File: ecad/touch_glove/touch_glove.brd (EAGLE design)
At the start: 80 x 38.4 mm, 376 parts, among them IC1 DRV8662, J1 VERT MALE 2.54MM, J2 VERT MALE 2.54MM, J3 VERT MALE 2.54MM, J4 VERT MALE 2.54MM, J5 VERT MALE 2.54MM, J6 PTH VERT MALE, J7 PTH VERT MALE, J8 PTH VERT MALE, J9 PTH VERT MALE, Q1 MCH3474 4A/30V, Q2 MCH3474 4A/30V, Q3 MCH3474 4A/30V, Q4 MCH3474 4A/30V, Q5 MCH3474 4A/30V, Q6 MCH3474 4A/30V, SW1 4A/28V, SW2 25mA/24V

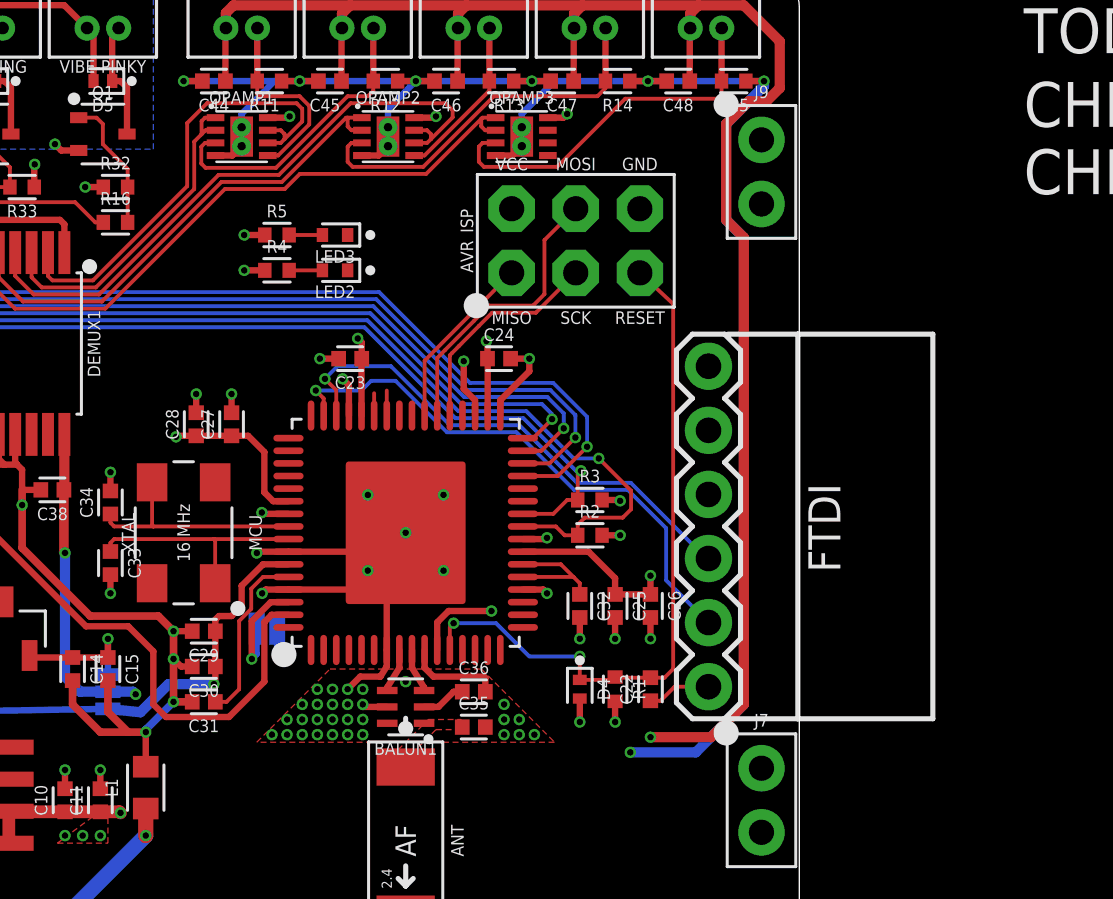
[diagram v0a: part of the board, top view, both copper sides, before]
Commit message: Create mcu to unity example code.  Create schematics for master thesis.  Edit robotic arm and touch glove pcb.
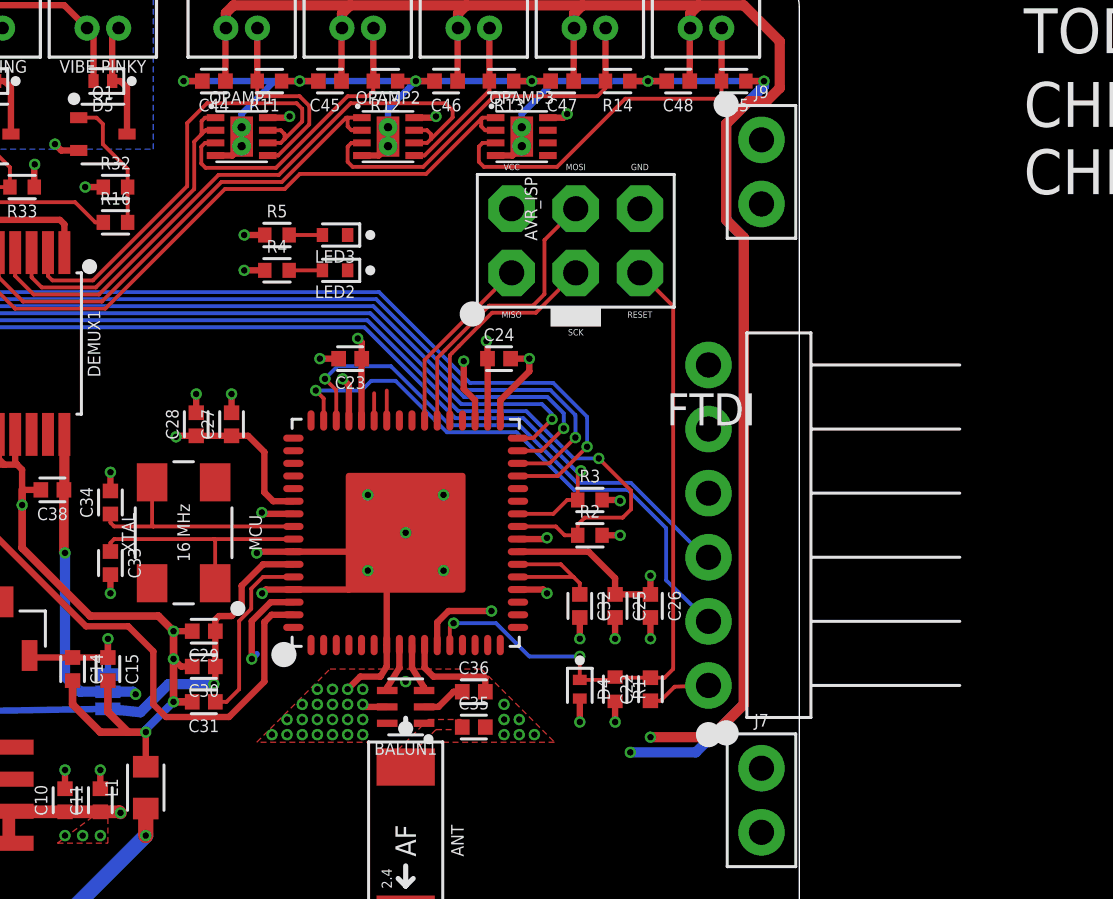
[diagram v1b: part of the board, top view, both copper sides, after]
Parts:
- removed JP2: JUMPER_SMD_2-PAD_NO_SILK, _connectors:SMT-JUMPER_2_NO_SILK
- AVR_ISP: value PTH VERT MALE -> AVR ISP; device _connectors:HDRV6W64P254_2X3_762X483X838B_AVR-ISP -> _connectors:HDRV6W64P254_2X3_762X508X838B
- FTDI: value FTDI -> PTH RA VERT MALE; device _connectors:FTDI_BASIC-6PIN-MALE-RA -> _connectors:HDRRA6W64P254_1X6_1524X254X254B_FTDI
- moved AVR_ISP 2.84 mm to (71.1, 27.9)
- turned FTDI to 90 degrees
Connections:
- removed net AREF: JP2.2, MCU.62
- net A1.8V: now also MCU.62
- net VSENSOR: no longer JP2.1
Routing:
- net AREF: track 4.55 -> 0.00 mm, vias 1 -> 0
- net A1.8V: track 5.30 -> 9.04 mm, vias 1 -> 2
- net GND: track 65.9 -> 66.9 mm
- net VSENSOR: track 138.6 -> 137.6 mm
- net VCC: track 50.3 -> 51.1 mm

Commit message: Create PCA9685Servo library.  Touch up Touch Glove PCB.  Major work completed on ET Extension.
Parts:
- removed C16, C19, C37, C49, C63, C64, C66, C67, C68, C69, C70, C76, C78, C80: 0.1uF/50V, _capacitors:CAPC1005X55_SMD-0402
- removed C17, C20, C71, C72, C73, C75, C77, C79: 10uF/6.3V, _capacitors:CAPC1005X55_SMD-0402
- removed C61: 0.1uF/25V, _capacitors:CAPC1608X95
- removed C62: 0.1uF/250V, _capacitors:CAPC2012X95_SMD-0805
- removed C65: 100uF/10V, _capacitors:CAPCP3216X160
- removed C74: 4.7uF/10V/0402, _capacitors:CAPC1005X55_SMD-0402
- removed ET_INDEX_PIXEL1-1, ET_INDEX_PIXEL1-10, ET_INDEX_PIXEL1-11, ET_INDEX_PIXEL1-12, ET_INDEX_PIXEL1-13, ET_INDEX_PIXEL1-14, ET_INDEX_PIXEL1-15, ET_INDEX_PIXEL1-16, ET_INDEX_PIXEL1-17, ET_INDEX_PIXEL1-18, ET_INDEX_PIXEL1-19, ET_INDEX_PIXEL1-2, ET_INDEX_PIXEL1-20, ET_INDEX_PIXEL1-3, ET_INDEX_PIXEL1-4, ET_INDEX_PIXEL1-5, ET_INDEX_PIXEL1-6, ET_INDEX_PIXEL1-7, ET_INDEX_PIXEL1-8, ET_INDEX_PIXEL1-9, ET_INDEX_PIXEL2-1, ET_INDEX_PIXEL2-10, ET_INDEX_PIXEL2-11, ET_INDEX_PIXEL2-12, ET_INDEX_PIXEL2-13, ET_INDEX_PIXEL2-14, ET_INDEX_PIXEL2-15, ET_INDEX_PIXEL2-16, ET_INDEX_PIXEL2-17, ET_INDEX_PIXEL2-18, ET_INDEX_PIXEL2-19, ET_INDEX_PIXEL2-2, ET_INDEX_PIXEL2-20, ET_INDEX_PIXEL2-3, ET_INDEX_PIXEL2-4, ET_INDEX_PIXEL2-5, ET_INDEX_PIXEL2-6, ET_INDEX_PIXEL2-7, ET_INDEX_PIXEL2-8, ET_INDEX_PIXEL2-9, ET_INDEX_PIXEL3-1, ET_INDEX_PIXEL3-10, ET_INDEX_PIXEL3-11, ET_INDEX_PIXEL3-12, ET_INDEX_PIXEL3-13, ET_INDEX_PIXEL3-14, ET_INDEX_PIXEL3-15, ET_INDEX_PIXEL3-16, ET_INDEX_PIXEL3-17, ET_INDEX_PIXEL3-18, ET_INDEX_PIXEL3-19, ET_INDEX_PIXEL3-2, ET_INDEX_PIXEL3-20, ET_INDEX_PIXEL3-3, ET_INDEX_PIXEL3-4, ET_INDEX_PIXEL3-5, ET_INDEX_PIXEL3-6, ET_INDEX_PIXEL3-7, ET_INDEX_PIXEL3-8, ET_INDEX_PIXEL3-9, ET_INDEX_PIXEL4-1, ET_INDEX_PIXEL4-10, ET_INDEX_PIXEL4-11, ET_INDEX_PIXEL4-12, ET_INDEX_PIXEL4-13, ET_INDEX_PIXEL4-14, ET_INDEX_PIXEL4-15, ET_INDEX_PIXEL4-16, ET_INDEX_PIXEL4-17, ET_INDEX_PIXEL4-18, ET_INDEX_PIXEL4-19, ET_INDEX_PIXEL4-2, ET_INDEX_PIXEL4-20, ET_INDEX_PIXEL4-3, ET_INDEX_PIXEL4-4, ET_INDEX_PIXEL4-5, ET_INDEX_PIXEL4-6, ET_INDEX_PIXEL4-7, ET_INDEX_PIXEL4-8, ET_INDEX_PIXEL4-9: SPST-NO 170mA 250V, _relay:SOP254P609X203-4
- removed IC1: DRV8662, _special:QFN50P400X400X100-21T270
- removed J1, J2, J3, J4, J5: VERT MALE 2.54MM, _connectors:HDRV16W64P254_1X16_4064X254X838B
- removed L3: 4.7uH/1.4A, _inductors:INDC2520X100
- removed L4: 10uH/380mA, _inductors:INDC1608X60-0603
- removed NFET1: 2N7002DW, _transistors:SOT65P230X110-6
- removed OPAMP4: TLV2361_GP_20MA_7MHZ, _op_amps:SOT95P280X145-5
- removed POT1: 100K, _resistors:POTENTIOMETER_SQ-L5-W4.5-H2.3
- removed PWM_DRIVER2, PWM_DRIVER3, PWM_DRIVER4, PWM_DRIVER5, PWM_DRIVER6: PCA9685, _special:SOP65P650X110-28
- removed R100, R101, R102, R103, R104, R105, R106, R107, R108, R109, R110, R111, R112, R113, R114, R115, R116, R117, R118, R119, R120, R121, R122, R123, R124, R125, R126, R127, R128, R129, R130, R131, R132, R133, R134, R135, R49, R57, R58, R59, R60, R61, R62, R63, R64, R65, R66, R67, R68, R69, R70, R71, R72, R73, R74, R75, R76, R77, R78, R79, R80, R81, R82, R83, R84, R85, R86, R87, R88, R89, R90, R91, R92, R93, R94, R95, R96, R97, R98, R99: 1K, _resistors:RESC1005X35_SMD-0402
- removed R136, R137, R54, R55, R56: 10K, _resistors:RESC1005X35_SMD-0402
- removed R16, R17, R18, R19, R20, R21, R22, R23, R24, R25, R26, R27, R28, R29, R30, R31: 100, _resistors:RESC1005X35_SMD-0402
- removed R50: 768K, _resistors:RESC1005X35_SMD-0402
- removed R51: 35.7K, _resistors:RESC1005X35_SMD-0402
- removed R52: 20K, _resistors:RESC1005X35_SMD-0402
- removed R53: 41.2K, _resistors:RESC1005X35_SMD-0402
- removed REXT: 7.5K, _resistors:RESC1005X35_SMD-0402
- removed SW2: 25mA/24V, _switches:SW_SLIDE_ARRAY-3_L9.6-W7.5-H4.5
- removed VREG-MCU1: TPS76833QDR 1A/3.3V, _ic_power:SOIC127P600X265-8
- removed VREG2: NCP1729 50mA, _ic_power:SOT95P275X100-6
- removed VREG3: TPS62202 300mA 1.8V, _ic_power:SOT95P280X145-5
- moved C8 3.04 mm to (22.0, 13.6)
- moved C9 3.03 mm to (22.0, 14.9)
- moved C2 3.00 mm to (23.0, 10.6)
- moved VREG-TEC 3.00 mm to (15.3, 19.8)
- moved D3 2.90 mm to (24.4, 19.8)
- moved C18 2.83 mm to (32.1, 17.4), turned to 180 degrees
- moved VREG-VIBE 2.38 mm to (30.3, 12.4)
- moved C3 2.30 mm to (30.3, 7.40)
- moved C7 2.30 mm to (33.9, 8.70)
- moved U$1 2.30 mm to (33.2, 7.00)
- moved C6 2.30 mm to (33.9, 7.40)
- moved R48 2.21 mm to (37.0, 8.20)
- moved LED1 2.20 mm to (37.0, 6.00)
- moved D2 2.18 mm to (35.9, 12.4)
- moved C50 1.94 mm to (41.4, 19.6)
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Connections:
- net AVCC renamed A3.3V
- removed net -1.8V: C72.1, OPAMP4.2, VREG2.1
- removed net C+: C71.1, VREG2.6
- removed net C-: C71.2, VREG2.3
- removed net EN: IC1.20, R54.2, SW2.S3
- removed net FB: IC1.3, R50.1, R51.2, R52.2, R53.2
- removed net GAIN0: IC1.18, NFET1.5, R55.2, SW2.S2
- removed net GAIN1: IC1.19, NFET1.2, R56.2, SW2.S1
- removed net IN+: C64.1, OPAMP4.4, POT1.1, POT1.2, R136.2
- removed net INDEX_IN1-1: ET_INDEX_PIXEL1-1.1, ET_INDEX_PIXEL1-13.1, ET_INDEX_PIXEL1-17.1, ET_INDEX_PIXEL1-5.1, ET_INDEX_PIXEL1-9.1, PWM_DRIVER2.6, PWM_DRIVER3.6, PWM_DRIVER4.6, PWM_DRIVER5.6, PWM_DRIVER6.6
- removed net INDEX_IN1-2: ET_INDEX_PIXEL1-10.1, ET_INDEX_PIXEL1-14.1, ET_INDEX_PIXEL1-18.1, ET_INDEX_PIXEL1-2.1, ET_INDEX_PIXEL1-6.1, PWM_DRIVER2.7, PWM_DRIVER3.7, PWM_DRIVER4.7, PWM_DRIVER5.7, PWM_DRIVER6.7
- removed net INDEX_IN1-3: ET_INDEX_PIXEL1-11.1, ET_INDEX_PIXEL1-15.1, ET_INDEX_PIXEL1-19.1, ET_INDEX_PIXEL1-3.1, ET_INDEX_PIXEL1-7.1, PWM_DRIVER2.8, PWM_DRIVER3.8, PWM_DRIVER4.8, PWM_DRIVER5.8, PWM_DRIVER6.8
- removed net INDEX_IN1-4: ET_INDEX_PIXEL1-12.1, ET_INDEX_PIXEL1-16.1, ET_INDEX_PIXEL1-20.1, ET_INDEX_PIXEL1-4.1, ET_INDEX_PIXEL1-8.1, PWM_DRIVER2.9, PWM_DRIVER3.9, PWM_DRIVER4.9, PWM_DRIVER5.9, PWM_DRIVER6.9
- removed net INDEX_IN2-1: ET_INDEX_PIXEL2-1.1, ET_INDEX_PIXEL2-11.1, ET_INDEX_PIXEL2-15.1, ET_INDEX_PIXEL2-19.1, ET_INDEX_PIXEL2-7.1, PWM_DRIVER2.10, PWM_DRIVER3.10, PWM_DRIVER4.10, PWM_DRIVER5.10, PWM_DRIVER6.10
- removed net INDEX_IN2-2: ET_INDEX_PIXEL2-10.1, ET_INDEX_PIXEL2-14.1, ET_INDEX_PIXEL2-18.1, ET_INDEX_PIXEL2-2.1, ET_INDEX_PIXEL2-6.1, PWM_DRIVER2.11, PWM_DRIVER3.11, PWM_DRIVER4.11, PWM_DRIVER5.11, PWM_DRIVER6.11
- removed net INDEX_IN2-3: ET_INDEX_PIXEL2-13.1, ET_INDEX_PIXEL2-17.1, ET_INDEX_PIXEL2-3.1, ET_INDEX_PIXEL2-5.1, ET_INDEX_PIXEL2-9.1, PWM_DRIVER2.12, PWM_DRIVER3.12, PWM_DRIVER4.12, PWM_DRIVER5.12, PWM_DRIVER6.12
- removed net INDEX_IN2-4: ET_INDEX_PIXEL2-12.1, ET_INDEX_PIXEL2-16.1, ET_INDEX_PIXEL2-20.1, ET_INDEX_PIXEL2-4.1, ET_INDEX_PIXEL2-8.1, PWM_DRIVER2.13, PWM_DRIVER3.13, PWM_DRIVER4.13, PWM_DRIVER5.13, PWM_DRIVER6.13
- removed net INDEX_IN3-1: ET_INDEX_PIXEL3-1.1, ET_INDEX_PIXEL3-13.1, ET_INDEX_PIXEL3-17.1, ET_INDEX_PIXEL3-5.1, ET_INDEX_PIXEL3-9.1, PWM_DRIVER2.15, PWM_DRIVER3.15, PWM_DRIVER4.15, PWM_DRIVER5.15, PWM_DRIVER6.15
- removed net INDEX_IN3-2: ET_INDEX_PIXEL3-10.1, ET_INDEX_PIXEL3-14.1, ET_INDEX_PIXEL3-18.1, ET_INDEX_PIXEL3-2.1, ET_INDEX_PIXEL3-6.1, PWM_DRIVER2.16, PWM_DRIVER3.16, PWM_DRIVER4.16, PWM_DRIVER5.16, PWM_DRIVER6.16
- removed net INDEX_IN3-3: ET_INDEX_PIXEL3-11.1, ET_INDEX_PIXEL3-15.1, ET_INDEX_PIXEL3-19.1, ET_INDEX_PIXEL3-3.1, ET_INDEX_PIXEL3-7.1, PWM_DRIVER2.17, PWM_DRIVER3.17, PWM_DRIVER4.17, PWM_DRIVER5.17, PWM_DRIVER6.17
- removed net INDEX_IN3-4: ET_INDEX_PIXEL3-12.1, ET_INDEX_PIXEL3-16.1, ET_INDEX_PIXEL3-20.1, ET_INDEX_PIXEL3-4.1, ET_INDEX_PIXEL3-8.1, PWM_DRIVER2.18, PWM_DRIVER3.18, PWM_DRIVER4.18, PWM_DRIVER5.18, PWM_DRIVER6.18
- removed net INDEX_IN4-1: ET_INDEX_PIXEL4-1.1, ET_INDEX_PIXEL4-13.1, ET_INDEX_PIXEL4-17.1, ET_INDEX_PIXEL4-5.1, ET_INDEX_PIXEL4-9.1, PWM_DRIVER2.19, PWM_DRIVER3.19, PWM_DRIVER4.19, PWM_DRIVER5.19, PWM_DRIVER6.19
- removed net INDEX_IN4-2: ET_INDEX_PIXEL4-10.1, ET_INDEX_PIXEL4-14.1, ET_INDEX_PIXEL4-18.1, ET_INDEX_PIXEL4-2.1, ET_INDEX_PIXEL4-6.1, PWM_DRIVER2.20, PWM_DRIVER3.20, PWM_DRIVER4.20, PWM_DRIVER5.20, PWM_DRIVER6.20
- removed net INDEX_IN4-3: ET_INDEX_PIXEL4-11.1, ET_INDEX_PIXEL4-15.1, ET_INDEX_PIXEL4-19.1, ET_INDEX_PIXEL4-3.1, ET_INDEX_PIXEL4-7.1, PWM_DRIVER2.21, PWM_DRIVER3.21, PWM_DRIVER4.21, PWM_DRIVER5.21, PWM_DRIVER6.21
- removed net INDEX_IN4-4: ET_INDEX_PIXEL4-12.1, ET_INDEX_PIXEL4-16.1, ET_INDEX_PIXEL4-20.1, ET_INDEX_PIXEL4-4.1, ET_INDEX_PIXEL4-8.1, PWM_DRIVER2.22, PWM_DRIVER3.22, PWM_DRIVER4.22, PWM_DRIVER5.22, PWM_DRIVER6.22
- removed net INDEX_OUT1-1: ET_INDEX_PIXEL1-1.3, ET_INDEX_PIXEL1-13.3, ET_INDEX_PIXEL1-17.3, ET_INDEX_PIXEL1-5.3, ET_INDEX_PIXEL1-9.3, J1.1, J2.1, J3.1, J4.1, J5.1
- removed net INDEX_OUT1-2: ET_INDEX_PIXEL1-10.3, ET_INDEX_PIXEL1-14.3, ET_INDEX_PIXEL1-18.3, ET_INDEX_PIXEL1-2.3, ET_INDEX_PIXEL1-6.3
- removed net INDEX_OUT1-3: ET_INDEX_PIXEL1-11.3, ET_INDEX_PIXEL1-15.3, ET_INDEX_PIXEL1-19.3, ET_INDEX_PIXEL1-3.3, ET_INDEX_PIXEL1-7.3
- removed net INDEX_OUT1-4: ET_INDEX_PIXEL1-12.3, ET_INDEX_PIXEL1-16.3, ET_INDEX_PIXEL1-20.3, ET_INDEX_PIXEL1-4.3, ET_INDEX_PIXEL1-8.3
- removed net INDEX_OUT2-1: ET_INDEX_PIXEL2-1.3, ET_INDEX_PIXEL2-11.3, ET_INDEX_PIXEL2-15.3, ET_INDEX_PIXEL2-19.3, ET_INDEX_PIXEL2-7.3
- removed net INDEX_OUT2-2: ET_INDEX_PIXEL2-10.3, ET_INDEX_PIXEL2-14.3, ET_INDEX_PIXEL2-18.3, ET_INDEX_PIXEL2-2.3, ET_INDEX_PIXEL2-6.3
- removed net INDEX_OUT2-3: ET_INDEX_PIXEL2-13.3, ET_INDEX_PIXEL2-17.3, ET_INDEX_PIXEL2-3.3, ET_INDEX_PIXEL2-5.3, ET_INDEX_PIXEL2-9.3
- removed net INDEX_OUT2-4: ET_INDEX_PIXEL2-12.3, ET_INDEX_PIXEL2-16.3, ET_INDEX_PIXEL2-20.3, ET_INDEX_PIXEL2-4.3, ET_INDEX_PIXEL2-8.3
- removed net INDEX_OUT3-1: ET_INDEX_PIXEL3-1.3, ET_INDEX_PIXEL3-13.3, ET_INDEX_PIXEL3-17.3, ET_INDEX_PIXEL3-5.3, ET_INDEX_PIXEL3-9.3
- removed net INDEX_OUT3-2: ET_INDEX_PIXEL3-10.3, ET_INDEX_PIXEL3-14.3, ET_INDEX_PIXEL3-18.3, ET_INDEX_PIXEL3-2.3, ET_INDEX_PIXEL3-6.3
- removed net INDEX_OUT3-3: ET_INDEX_PIXEL3-11.3, ET_INDEX_PIXEL3-15.3, ET_INDEX_PIXEL3-19.3, ET_INDEX_PIXEL3-3.3, ET_INDEX_PIXEL3-7.3
- removed net INDEX_OUT3-4: ET_INDEX_PIXEL3-12.3, ET_INDEX_PIXEL3-16.3, ET_INDEX_PIXEL3-20.3, ET_INDEX_PIXEL3-4.3, ET_INDEX_PIXEL3-8.3
- removed net INDEX_OUT4-1: ET_INDEX_PIXEL4-1.3, ET_INDEX_PIXEL4-13.3, ET_INDEX_PIXEL4-17.3, ET_INDEX_PIXEL4-5.3, ET_INDEX_PIXEL4-9.3
- removed net INDEX_OUT4-2: ET_INDEX_PIXEL4-10.3, ET_INDEX_PIXEL4-14.3, ET_INDEX_PIXEL4-18.3, ET_INDEX_PIXEL4-2.3, ET_INDEX_PIXEL4-6.3
- removed net INDEX_OUT4-3: ET_INDEX_PIXEL4-11.3, ET_INDEX_PIXEL4-15.3, ET_INDEX_PIXEL4-19.3, ET_INDEX_PIXEL4-3.3, ET_INDEX_PIXEL4-7.3
- removed net INDEX_OUT4-4: ET_INDEX_PIXEL4-12.3, ET_INDEX_PIXEL4-16.3, ET_INDEX_PIXEL4-20.3, ET_INDEX_PIXEL4-4.3, ET_INDEX_PIXEL4-8.3
- removed net N$10: HBRIDGE-INDEX.6, R24.2, R40.2
- removed net N$100: ET_INDEX_PIXEL3-12.2, R99.2
- removed net N$101: ET_INDEX_PIXEL4-9.2, R100.2
- removed net N$102: ET_INDEX_PIXEL4-10.2, R101.2
- removed net N$103: ET_INDEX_PIXEL4-11.2, R102.2
- removed net N$104: ET_INDEX_PIXEL4-12.2, R103.2
- removed net N$105: ET_INDEX_PIXEL1-13.2, R104.2
- removed net N$106: ET_INDEX_PIXEL1-14.2, R105.2
- removed net N$107: ET_INDEX_PIXEL1-15.2, R106.2
- removed net N$108: ET_INDEX_PIXEL1-16.2, R107.2
- removed net N$109: ET_INDEX_PIXEL2-15.2, R108.2
- removed net N$110: ET_INDEX_PIXEL2-14.2, R109.2
- removed net N$111: ET_INDEX_PIXEL2-13.2, R110.2
- removed net N$112: ET_INDEX_PIXEL2-16.2, R111.2
- removed net N$113: ET_INDEX_PIXEL3-13.2, R112.2
- removed net N$114: ET_INDEX_PIXEL3-14.2, R113.2
- removed net N$115: ET_INDEX_PIXEL3-15.2, R114.2
- removed net N$116: ET_INDEX_PIXEL3-16.2, R115.2
- removed net N$117: ET_INDEX_PIXEL4-13.2, R116.2
- removed net N$118: ET_INDEX_PIXEL4-14.2, R117.2
- removed net N$119: ET_INDEX_PIXEL4-15.2, R118.2
- removed net N$120: ET_INDEX_PIXEL4-16.2, R119.2
- removed net N$121: ET_INDEX_PIXEL1-17.2, R120.2
- removed net N$122: ET_INDEX_PIXEL1-18.2, R121.2
- removed net N$123: ET_INDEX_PIXEL1-19.2, R122.2
- removed net N$124: ET_INDEX_PIXEL1-20.2, R123.2
- removed net N$125: ET_INDEX_PIXEL2-19.2, R124.2
- removed net N$126: ET_INDEX_PIXEL2-18.2, R125.2
- removed net N$127: ET_INDEX_PIXEL2-17.2, R126.2
- removed net N$128: ET_INDEX_PIXEL2-20.2, R127.2
- removed net N$129: ET_INDEX_PIXEL3-17.2, R128.2
- removed net N$13: HBRIDGE-MIDDLE.5, R27.2, R43.2
- removed net N$130: ET_INDEX_PIXEL3-18.2, R129.2
- removed net N$131: ET_INDEX_PIXEL3-19.2, R130.2
- removed net N$132: ET_INDEX_PIXEL3-20.2, R131.2
- removed net N$133: ET_INDEX_PIXEL4-17.2, R132.2
- removed net N$134: ET_INDEX_PIXEL4-18.2, R133.2
- removed net N$135: ET_INDEX_PIXEL4-19.2, R134.2
- removed net N$136: ET_INDEX_PIXEL4-20.2, R135.2
- removed net N$137: L4.1, VREG3.5
- removed net N$138: OPAMP4.1, R136.1, R137.2
- removed net N$139: C76.1, OPAMP4.3, POT1.3
- removed net N$14: HBRIDGE-MIDDLE.6, R26.2, R42.2
- removed net N$19: HBRIDGE-RING.5, R29.2, R45.2
- removed net N$20: HBRIDGE-RING.6, R28.2, R44.2
- removed net N$21: Q4.1, R19.2, R35.2
- removed net N$22: Q5.1, R20.2, R36.2
- removed net N$25: HBRIDGE-PINKY.5, R31.2, R47.2
- removed net N$26: HBRIDGE-PINKY.6, R30.2, R46.2
- removed net N$28: Q1.1, R16.2, R32.2
- removed net N$29: HBRIDGE-THUMB.5, R23.2, R39.2
- removed net N$31: HBRIDGE-THUMB.6, R22.2, R38.2
- removed net N$32: Q6.1, R21.2, R37.2
- removed net N$33: ET_INDEX_PIXEL1-3.2, R58.2
- removed net N$39: ET_INDEX_PIXEL1-1.2, R49.2
- removed net N$42: IC1.7, IC1.8, L3.1
- removed net N$43: C49.1, IC1.1
- removed net N$44: C62.1, IC1.10, IC1.11, IC1.12, R50.2
- removed net N$48: IC1.15, REXT.2
- removed net N$49: NFET1.6, R52.1
- removed net N$51: NFET1.3, R53.1
- removed net N$52: C64.2, IC1.17
- removed net N$56: C63.2, IC1.16
- removed net N$57: ET_INDEX_PIXEL1-2.2, R57.2
- removed net N$58: ET_INDEX_PIXEL1-5.2, R72.2
- removed net N$59: ET_INDEX_PIXEL1-4.2, R59.2
- removed net N$60: ET_INDEX_PIXEL2-1.2, R60.2
- removed net N$61: ET_INDEX_PIXEL2-2.2, R61.2
- removed net N$64: ET_INDEX_PIXEL2-3.2, R62.2
- removed net N$65: ET_INDEX_PIXEL2-4.2, R63.2
- removed net N$66: ET_INDEX_PIXEL3-1.2, R64.2
- removed net N$67: ET_INDEX_PIXEL3-2.2, R65.2
- removed net N$68: ET_INDEX_PIXEL3-3.2, R66.2
- removed net N$69: ET_INDEX_PIXEL3-4.2, R67.2
- removed net N$7: Q2.1, R17.2, R33.2, VREG3.3
- removed net N$70: ET_INDEX_PIXEL4-1.2, R68.2
- removed net N$71: ET_INDEX_PIXEL4-2.2, R69.2
- removed net N$72: ET_INDEX_PIXEL4-3.2, R70.2
- removed net N$73: ET_INDEX_PIXEL4-4.2, R71.2
- removed net N$74: ET_INDEX_PIXEL1-6.2, R73.2
- removed net N$75: ET_INDEX_PIXEL1-7.2, R74.2
- removed net N$76: ET_INDEX_PIXEL1-8.2, R75.2
- removed net N$77: ET_INDEX_PIXEL2-7.2, R76.2
- removed net N$78: ET_INDEX_PIXEL2-6.2, R77.2
- removed net N$79: ET_INDEX_PIXEL2-5.2, R78.2
- removed net N$8: HBRIDGE-INDEX.5, R25.2, R41.2
- removed net N$80: ET_INDEX_PIXEL2-8.2, R79.2
- removed net N$81: ET_INDEX_PIXEL3-5.2, R80.2
- removed net N$82: ET_INDEX_PIXEL3-6.2, R81.2
- removed net N$83: ET_INDEX_PIXEL3-7.2, R82.2
- removed net N$84: ET_INDEX_PIXEL3-8.2, R83.2
- removed net N$85: ET_INDEX_PIXEL4-5.2, R84.2
- removed net N$86: ET_INDEX_PIXEL4-6.2, R85.2
- removed net N$87: ET_INDEX_PIXEL4-7.2, R86.2
- removed net N$88: ET_INDEX_PIXEL4-8.2, R87.2
- removed net N$89: ET_INDEX_PIXEL1-9.2, R88.2
- removed net N$9: Q3.1, R18.2, R34.2
- removed net N$90: ET_INDEX_PIXEL1-10.2, R89.2
- removed net N$91: ET_INDEX_PIXEL1-11.2, R90.2
- removed net N$92: ET_INDEX_PIXEL1-12.2, R91.2
- removed net N$93: ET_INDEX_PIXEL2-11.2, R92.2
- removed net N$94: ET_INDEX_PIXEL2-10.2, R93.2
- removed net N$95: ET_INDEX_PIXEL2-9.2, R94.2
- removed net N$96: ET_INDEX_PIXEL2-12.2, R95.2
- removed net N$97: ET_INDEX_PIXEL3-9.2, R96.2
- removed net N$98: ET_INDEX_PIXEL3-10.2, R97.2
- removed net N$99: ET_INDEX_PIXEL3-11.2, R98.2
- removed net V+: ET_INDEX_PIXEL1-1.4, ET_INDEX_PIXEL1-10.4, ET_INDEX_PIXEL1-11.4, ET_INDEX_PIXEL1-12.4, ET_INDEX_PIXEL1-13.4, ET_INDEX_PIXEL1-14.4, ET_INDEX_PIXEL1-15.4, ET_INDEX_PIXEL1-16.4, ET_INDEX_PIXEL1-17.4, ET_INDEX_PIXEL1-18.4, ET_INDEX_PIXEL1-19.4, ET_INDEX_PIXEL1-2.4, ET_INDEX_PIXEL1-20.4, ET_INDEX_PIXEL1-3.4, ET_INDEX_PIXEL1-4.4, ET_INDEX_PIXEL1-5.4, ET_INDEX_PIXEL1-6.4, ET_INDEX_PIXEL1-7.4, ET_INDEX_PIXEL1-8.4, ET_INDEX_PIXEL1-9.4, ET_INDEX_PIXEL2-1.4, ET_INDEX_PIXEL2-10.4, ET_INDEX_PIXEL2-11.4, ET_INDEX_PIXEL2-12.4, ET_INDEX_PIXEL2-13.4, ET_INDEX_PIXEL2-14.4, ET_INDEX_PIXEL2-15.4, ET_INDEX_PIXEL2-16.4, ET_INDEX_PIXEL2-17.4, ET_INDEX_PIXEL2-18.4, ET_INDEX_PIXEL2-19.4, ET_INDEX_PIXEL2-2.4, ET_INDEX_PIXEL2-20.4, ET_INDEX_PIXEL2-3.4, ET_INDEX_PIXEL2-4.4, ET_INDEX_PIXEL2-5.4, ET_INDEX_PIXEL2-6.4, ET_INDEX_PIXEL2-7.4, ET_INDEX_PIXEL2-8.4, ET_INDEX_PIXEL2-9.4, ET_INDEX_PIXEL3-1.4, ET_INDEX_PIXEL3-10.4, ET_INDEX_PIXEL3-11.4, ET_INDEX_PIXEL3-12.4, ET_INDEX_PIXEL3-13.4, ET_INDEX_PIXEL3-14.4, ET_INDEX_PIXEL3-15.4, ET_INDEX_PIXEL3-16.4, ET_INDEX_PIXEL3-17.4, ET_INDEX_PIXEL3-18.4, ET_INDEX_PIXEL3-19.4, ET_INDEX_PIXEL3-2.4, ET_INDEX_PIXEL3-20.4, ET_INDEX_PIXEL3-3.4, ET_INDEX_PIXEL3-4.4, ET_INDEX_PIXEL3-5.4, ET_INDEX_PIXEL3-6.4, ET_INDEX_PIXEL3-7.4, ET_INDEX_PIXEL3-8.4, ET_INDEX_PIXEL3-9.4, ET_INDEX_PIXEL4-1.4, ET_INDEX_PIXEL4-10.4, ET_INDEX_PIXEL4-11.4, ET_INDEX_PIXEL4-12.4, ET_INDEX_PIXEL4-13.4, ET_INDEX_PIXEL4-14.4, ET_INDEX_PIXEL4-15.4, ET_INDEX_PIXEL4-16.4, ET_INDEX_PIXEL4-17.4, ET_INDEX_PIXEL4-18.4, ET_INDEX_PIXEL4-19.4, ET_INDEX_PIXEL4-2.4, ET_INDEX_PIXEL4-20.4, ET_INDEX_PIXEL4-3.4, ET_INDEX_PIXEL4-4.4, ET_INDEX_PIXEL4-5.4, ET_INDEX_PIXEL4-6.4, ET_INDEX_PIXEL4-7.4, ET_INDEX_PIXEL4-8.4, ET_INDEX_PIXEL4-9.4, IC1.13
- removed net V-: IC1.14, J1.16, J2.16, J3.16, J4.16, J5.16
- net 1.8V: no longer C19.1, C20.1, C73.1, C75.1, L4.2, OPAMP4.5, VREG2.2, VREG2.5, VREG3.4
- net 3.3V: no longer C16.1, C17.1, C37.1, C61.1, C65.A, C74.1, C77.1, C78.1, IC1.2, L3.2, SW2.P1, SW2.P2, SW2.P3, VREG-MCU1.5, VREG-MCU1.6, VREG3.1
- net GND: no longer C37.2, C49.2, C61.2, C62.2, C63.1, C65.K, C66.2, C67.2, C68.2, C69.2, C70.2, C72.2, C73.2, C74.2, C75.2, C76.2, C77.2, C78.2, C79.2, C80.2, IC1.4, IC1.5, IC1.6, IC1.9, IC1.EP, IC1.P$1, IC1.P$2, IC1.P$3, IC1.P$4, NFET1.1, NFET1.4, PWM_DRIVER2.1, PWM_DRIVER2.14, PWM_DRIVER2.2, PWM_DRIVER2.23, PWM_DRIVER2.24, PWM_DRIVER2.25, PWM_DRIVER2.3, PWM_DRIVER2.4, PWM_DRIVER2.5, PWM_DRIVER3.1, PWM_DRIVER3.14, PWM_DRIVER3.2, PWM_DRIVER3.23, PWM_DRIVER3.24, PWM_DRIVER3.25, PWM_DRIVER3.3, PWM_DRIVER3.4, PWM_DRIVER3.5, PWM_DRIVER4.1, PWM_DRIVER4.14, PWM_DRIVER4.2, PWM_DRIVER4.23, PWM_DRIVER4.24, PWM_DRIVER4.25, PWM_DRIVER4.3, PWM_DRIVER4.4, PWM_DRIVER4.5, PWM_DRIVER5.1, PWM_DRIVER5.14, PWM_DRIVER5.2, PWM_DRIVER5.23, PWM_DRIVER5.24, PWM_DRIVER5.25, PWM_DRIVER5.3, PWM_DRIVER5.4, PWM_DRIVER5.5, PWM_DRIVER6.1, PWM_DRIVER6.14, PWM_DRIVER6.2, PWM_DRIVER6.23, PWM_DRIVER6.24, PWM_DRIVER6.25, PWM_DRIVER6.3, PWM_DRIVER6.4, PWM_DRIVER6.5, R100.1, R101.1, R102.1, R103.1, R104.1, R105.1, R106.1, R107.1, R108.1, R109.1, R110.1, R111.1, R112.1, R113.1, R114.1, R115.1, R116.1, R117.1, R118.1, R119.1, R120.1, R121.1, R122.1, R123.1, R124.1, R125.1, R126.1, R127.1, R128.1, R129.1, R130.1, R131.1, R132.1, R133.1, R134.1, R135.1, R137.1, R49.1, R51.1, R54.1, R55.1, R56.1, R57.1, R58.1, R59.1, R60.1, R61.1, R62.1, R63.1, R64.1, R65.1, R66.1, R67.1, R68.1, R69.1, R70.1, R71.1, R72.1, R73.1, R74.1, R75.1, R76.1, R77.1, R78.1, R79.1, R80.1, R81.1, R82.1, R83.1, R84.1, R85.1, R86.1, R87.1, R88.1, R89.1, R90.1, R91.1, R92.1, R93.1, R94.1, R95.1, R96.1, R97.1, R98.1, R99.1, REXT.1, VREG-MCU1.1, VREG-MCU1.2, VREG2.4, VREG3.2
- net NGND: no longer C16.2, C17.2, C19.2, C20.2
- net SCL: no longer PWM_DRIVER2.26, PWM_DRIVER3.26, PWM_DRIVER4.26, PWM_DRIVER5.26, PWM_DRIVER6.26
- net SDA: no longer PWM_DRIVER2.27, PWM_DRIVER3.27, PWM_DRIVER4.27, PWM_DRIVER5.27, PWM_DRIVER6.27
- net TEC-INDEX-COLD: now also HBRIDGE-INDEX.5, R41.2; no longer R25.1
- net TEC-INDEX-HOT: now also HBRIDGE-INDEX.6, R40.2; no longer R24.1
- net TEC-MIDDLE-COLD: now also HBRIDGE-MIDDLE.5, R43.2; no longer R27.1
- net TEC-MIDDLE-HOT: now also HBRIDGE-MIDDLE.6, R42.2; no longer R26.1
- net TEC-PINKY-COLD: now also HBRIDGE-PINKY.5, R47.2; no longer R31.1
- net TEC-PINKY-HOT: now also HBRIDGE-PINKY.6, R46.2; no longer R30.1
- net TEC-RING-COLD: now also HBRIDGE-RING.5, R45.2; no longer R29.1
- net TEC-RING-HOT: now also HBRIDGE-RING.6, R44.2; no longer R28.1
- net TEC-THUMB-COLD: now also HBRIDGE-THUMB.5, R39.2; no longer R23.1
- net TEC-THUMB-HOT: now also HBRIDGE-THUMB.6, R38.2; no longer R22.1
- net VBAT: no longer C79.1, C80.1, VREG-MCU1.3, VREG-MCU1.4
- net VCC: no longer C66.1, C67.1, C68.1, C69.1, C70.1, PWM_DRIVER2.28, PWM_DRIVER3.28, PWM_DRIVER4.28, PWM_DRIVER5.28, PWM_DRIVER6.28
- net VIBE-INDEX: now also Q4.1, R35.2; no longer R19.1
- net VIBE-MIDDLE: now also Q3.1, R34.2; no longer R18.1
- net VIBE-PALM: now also Q6.1, R37.2; no longer R21.1
- net VIBE-PINKY: now also Q1.1, R32.2; no longer R16.1
- net VIBE-RING: now also Q2.1, R33.2; no longer R17.1
- net VIBE-THUMB: now also Q5.1, R36.2; no longer R20.1
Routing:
- net N$29: track 31.7 -> 0.00 mm
- net TEC-THUMB-COLD: track 6.06 -> 37.3 mm
- net N$31: track 28.6 -> 0.00 mm
- net TEC-THUMB-HOT: track 7.89 -> 35.8 mm
- net N$8: track 24.9 -> 0.00 mm
- net TEC-INDEX-COLD: track 9.56 -> 33.8 mm
- net N$14: track 23.3 -> 0.00 mm
- net TEC-MIDDLE-HOT: track 6.82 -> 29.3 mm
- net N$10: track 21.8 -> 0.00 mm
- net TEC-INDEX-HOT: track 11.9 -> 32.6 mm
- net N$19: track 19.6 -> 0.00 mm
- net TEC-RING-COLD: track 8.37 -> 27.2 mm
- net N$13: track 18.0 -> 0.00 mm
- net TEC-MIDDLE-COLD: track 13.6 -> 30.5 mm
- net N$20: track 16.4 -> 0.00 mm
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- removed copper zone on layer 1, net VCC
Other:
- board text removed: "CHECK new pins used (Demux) CHECK RESISTOR VALUE FOR NEW FLEX SENSORS"
- board text removed: "TODO"

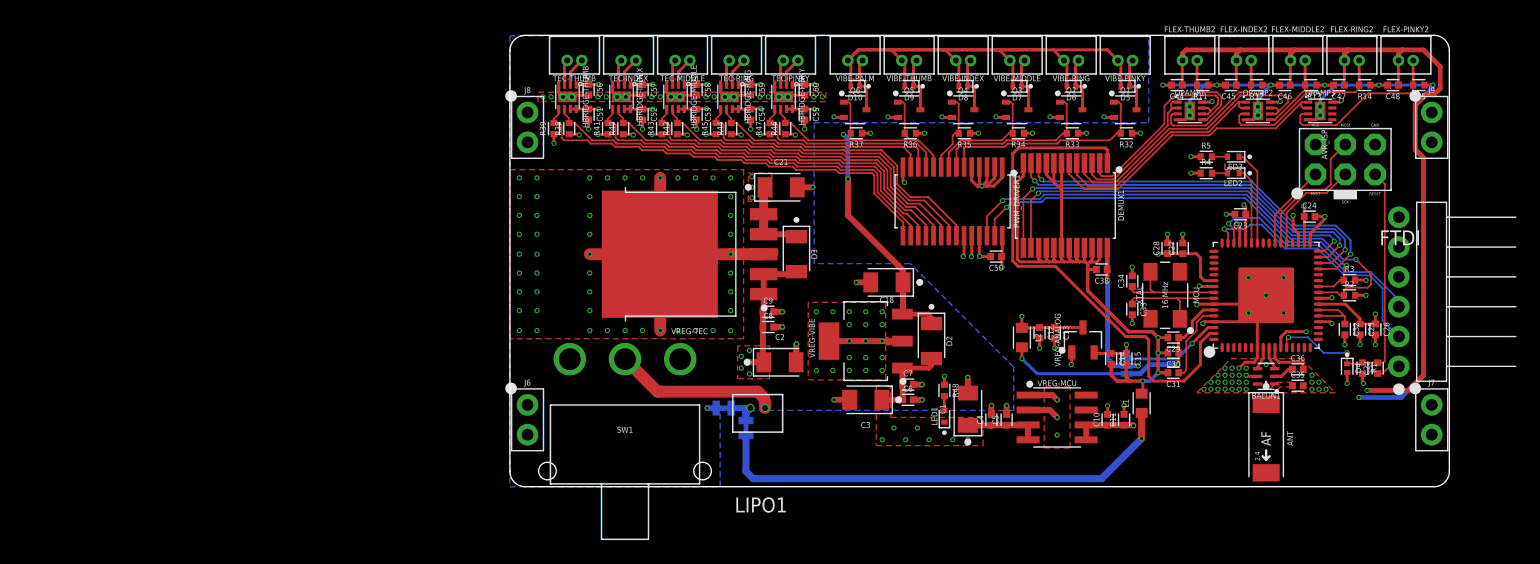
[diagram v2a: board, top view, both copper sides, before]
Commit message: Complete iteration of ET Extension and Touch Glove.  Verify PCA9685Servo library works and made appropriate changes in robotic arm master code.
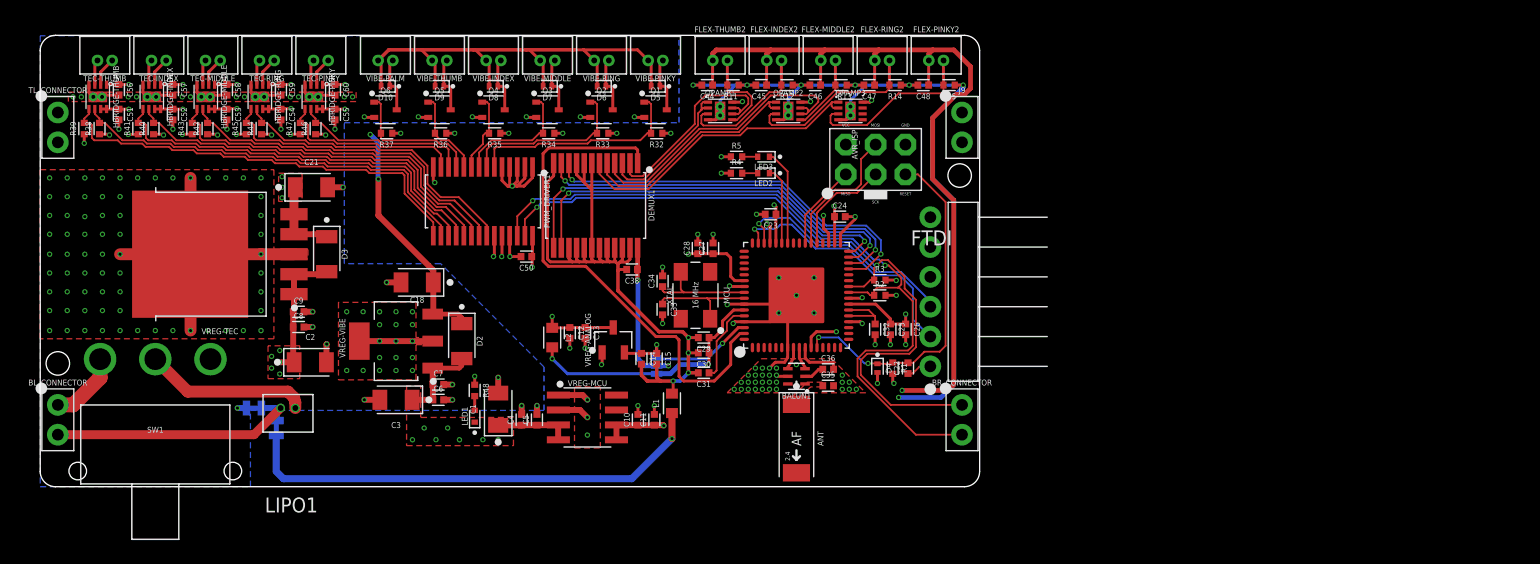
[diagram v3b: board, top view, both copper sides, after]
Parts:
- removed J6, J7, J8: PTH VERT MALE, _connectors:HDRV2W64P254_1X2_508X254X838B
- added BL_CONNECTOR, BR_CONNECTOR, TL_CONNECTOR: PTH VERT MALE, _connectors:HDRV2W64P254_1X2_508X254X838B
- moved U$1 42.4 mm to (-9.10, 4.50)
- moved ANT 40.0 mm to (24.4, 4.10)
- moved BALUN1 40.0 mm to (24.4, 9.40)
- moved C22 40.0 mm to (33.9, 10.1)
- moved C25 40.0 mm to (32.4, 13.4)
- moved MCU 40.0 mm to (24.4, 16.3)
- moved R15 40.0 mm to (37.4, 34.2)
- moved AVR_ISP 40.0 mm to (31.1, 27.9)
- moved BR_ANALOG 40.0 mm to (-19.9, 5.00)
- moved BR_NOISE 40.0 mm to (-21.8, 6.70)
- moved C1 40.0 mm to (-1.00, 6.60)
- moved C10 40.0 mm to (10.9, 5.70)
- moved C11 40.0 mm to (12.3, 5.70)
- moved C12 40.0 mm to (5.10, 13.1)
- moved C13 40.0 mm to (6.40, 13.1)
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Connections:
- net GND: now also BL_CONNECTOR.2
- net NGND: now also TL_CONNECTOR.1, TL_CONNECTOR.2; no longer J8.1, J8.2
- net SCL: now also BR_CONNECTOR.2
- net SDA: now also BR_CONNECTOR.1
- net VBAT: now also BL_CONNECTOR.1
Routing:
- net SDA: track 38.2 -> 63.9 mm
- net SCL: track 44.0 -> 66.9 mm
- net GND: track 70.1 -> 90.1 mm
- net VBAT: track 25.7 -> 31.8 mm
- net RESET: track 27.0 -> 30.0 mm
- net AGND: track 200.4 -> 201.8 mm
- net VSENSOR: track 134.3 -> 135.7 mm
- net NGND: vias 100 -> 118
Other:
- board text added: "Designed by:"
- board text removed: "Designed by: &"

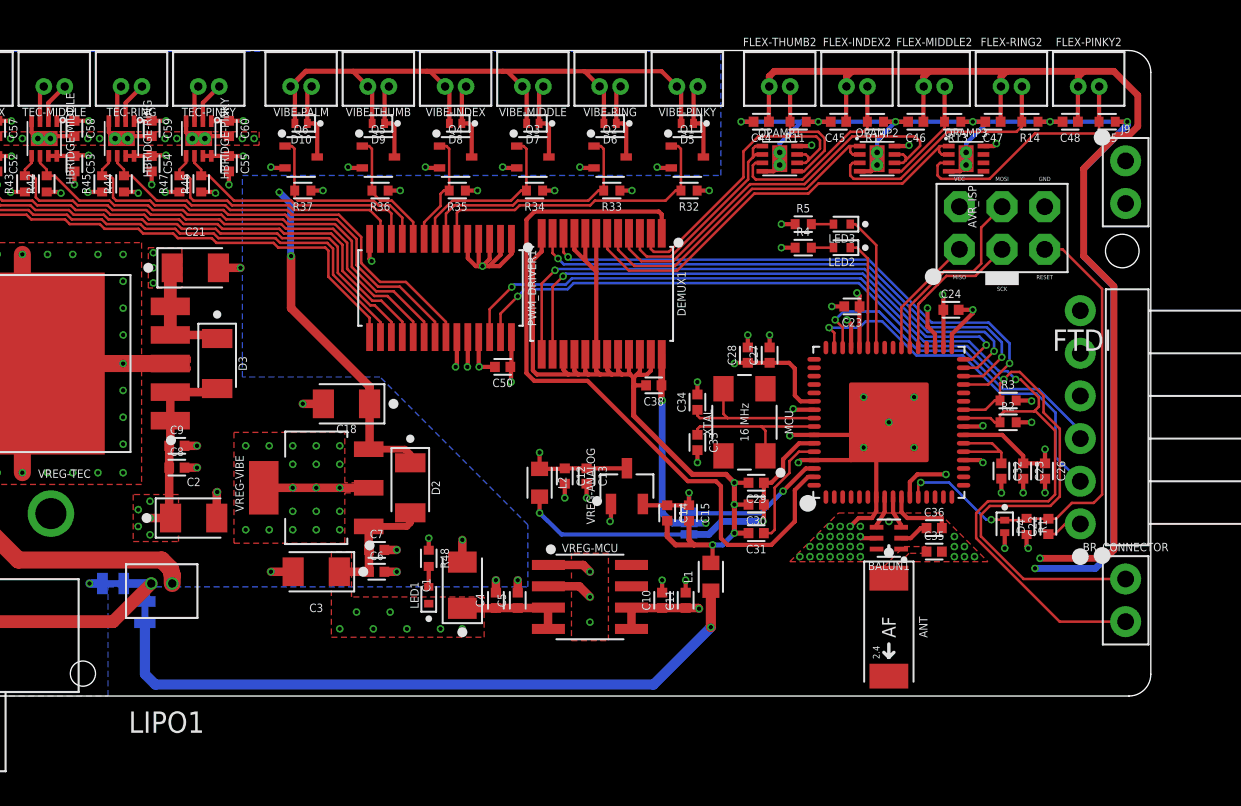
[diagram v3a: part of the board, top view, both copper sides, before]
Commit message: Fix sizing of some text on board.  Clean up schematic.
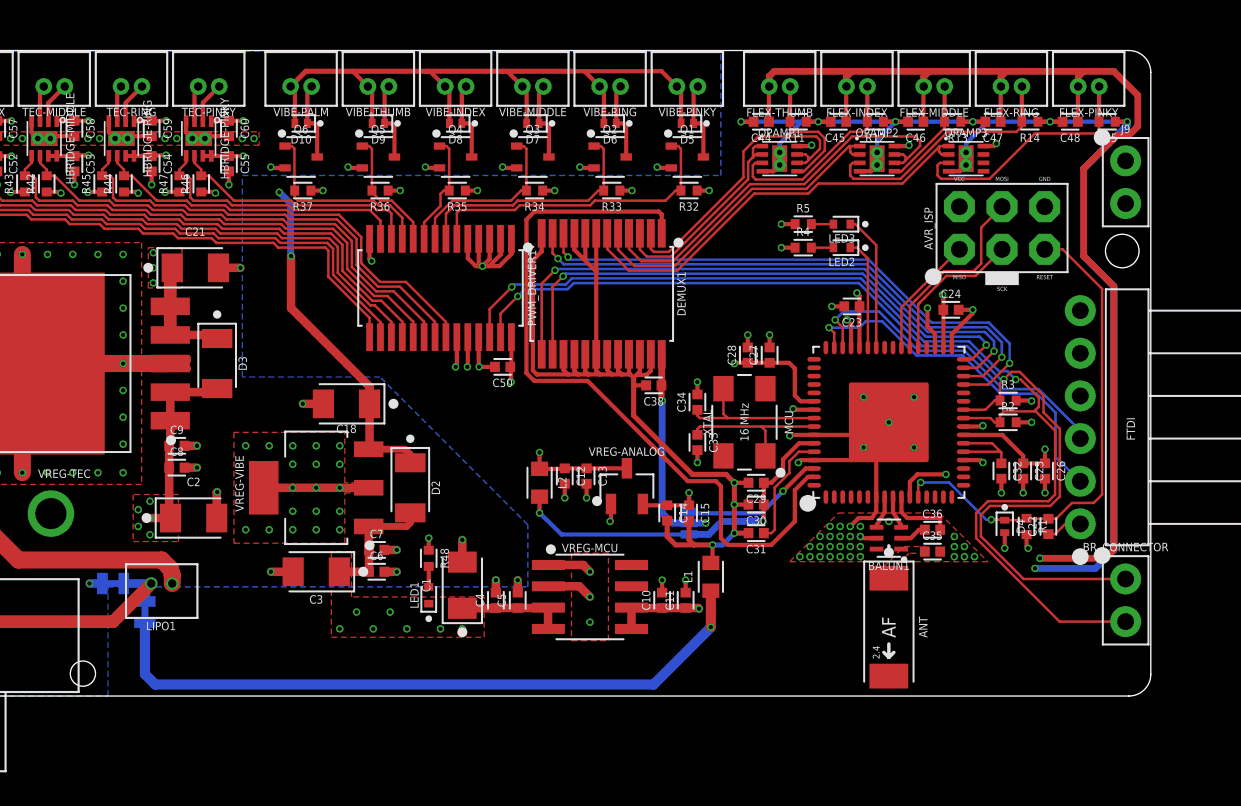
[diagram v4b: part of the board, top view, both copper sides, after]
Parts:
- moved C36 0.14 mm to (27.0, 9.90)
- moved C35 0.10 mm to (27.0, 8.60)
- renumbered FLEX-INDEX2 to FLEX-INDEX, FLEX-MIDDLE2 to FLEX-MIDDLE, FLEX-PINKY2 to FLEX-PINKY, FLEX-RING2 to FLEX-RING, FLEX-THUMB2 to FLEX-THUMB
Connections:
- net FLEX-INDEX2 renamed FLEX-INDEX
- net FLEX-MIDDLE2 renamed FLEX-MIDDLE
- net FLEX-PINKY2 renamed FLEX-PINKY
- net FLEX-RING2 renamed FLEX-RING
- net FLEX-THUMB2 renamed FLEX-THUMB
